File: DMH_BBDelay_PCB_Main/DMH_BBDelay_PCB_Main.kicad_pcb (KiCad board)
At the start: 2 copper layers, 99 x 175 mm, 0 parts

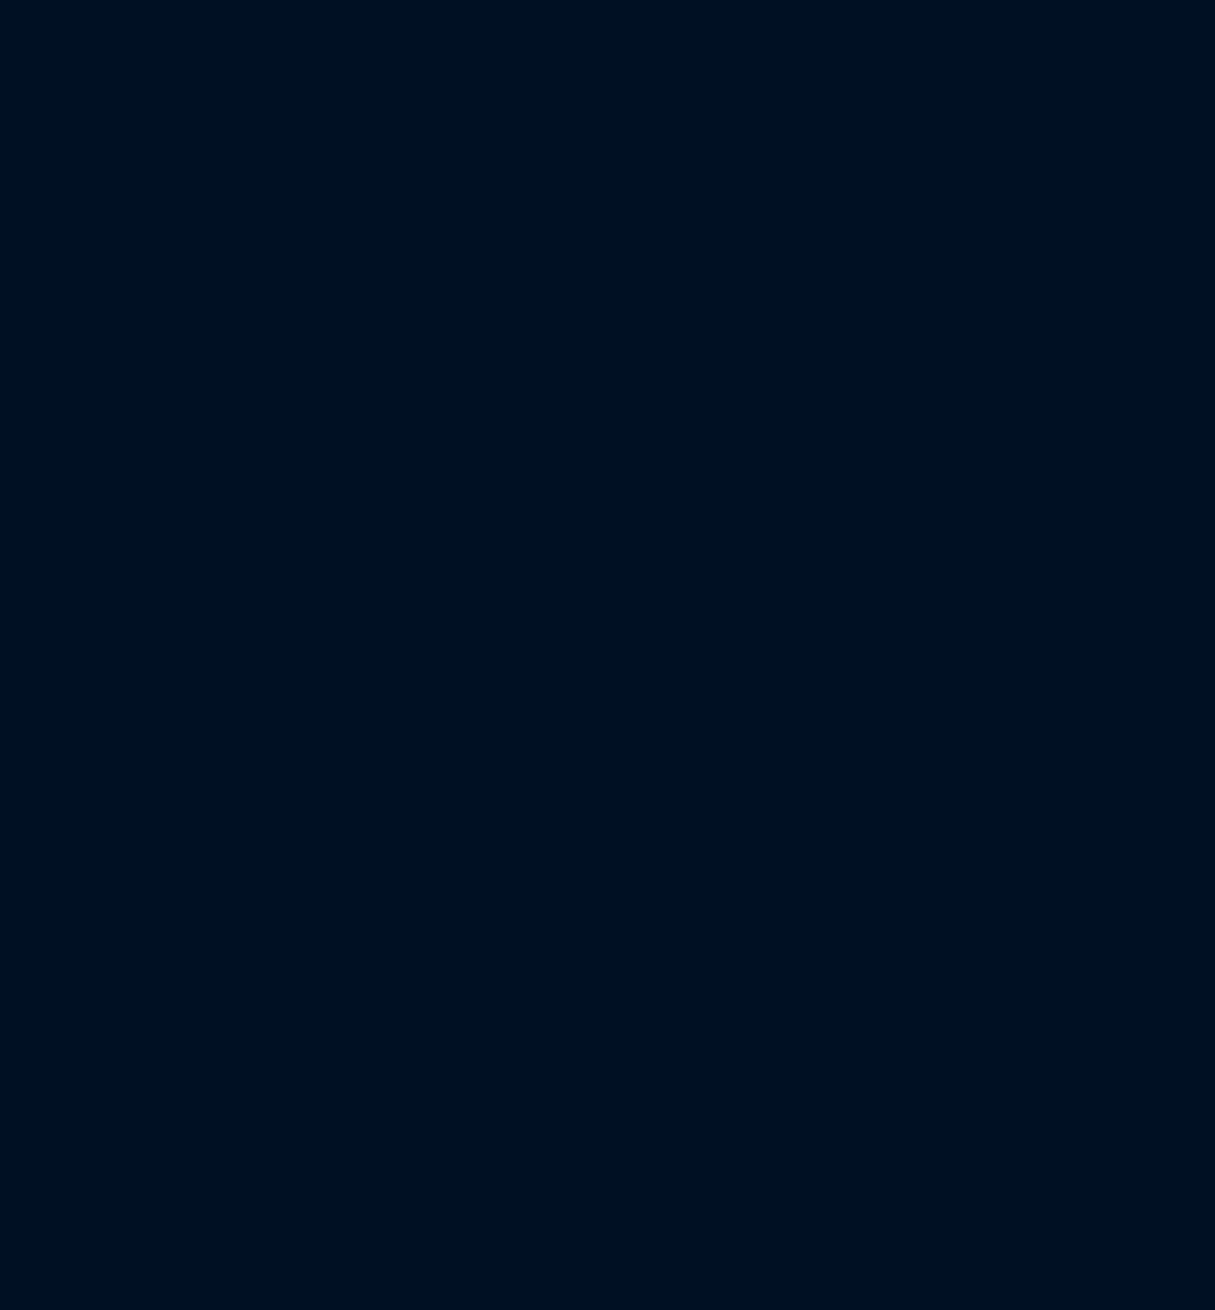
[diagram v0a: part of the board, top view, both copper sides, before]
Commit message: Added connectors for submodules
... and marked which components are not in Main PCB
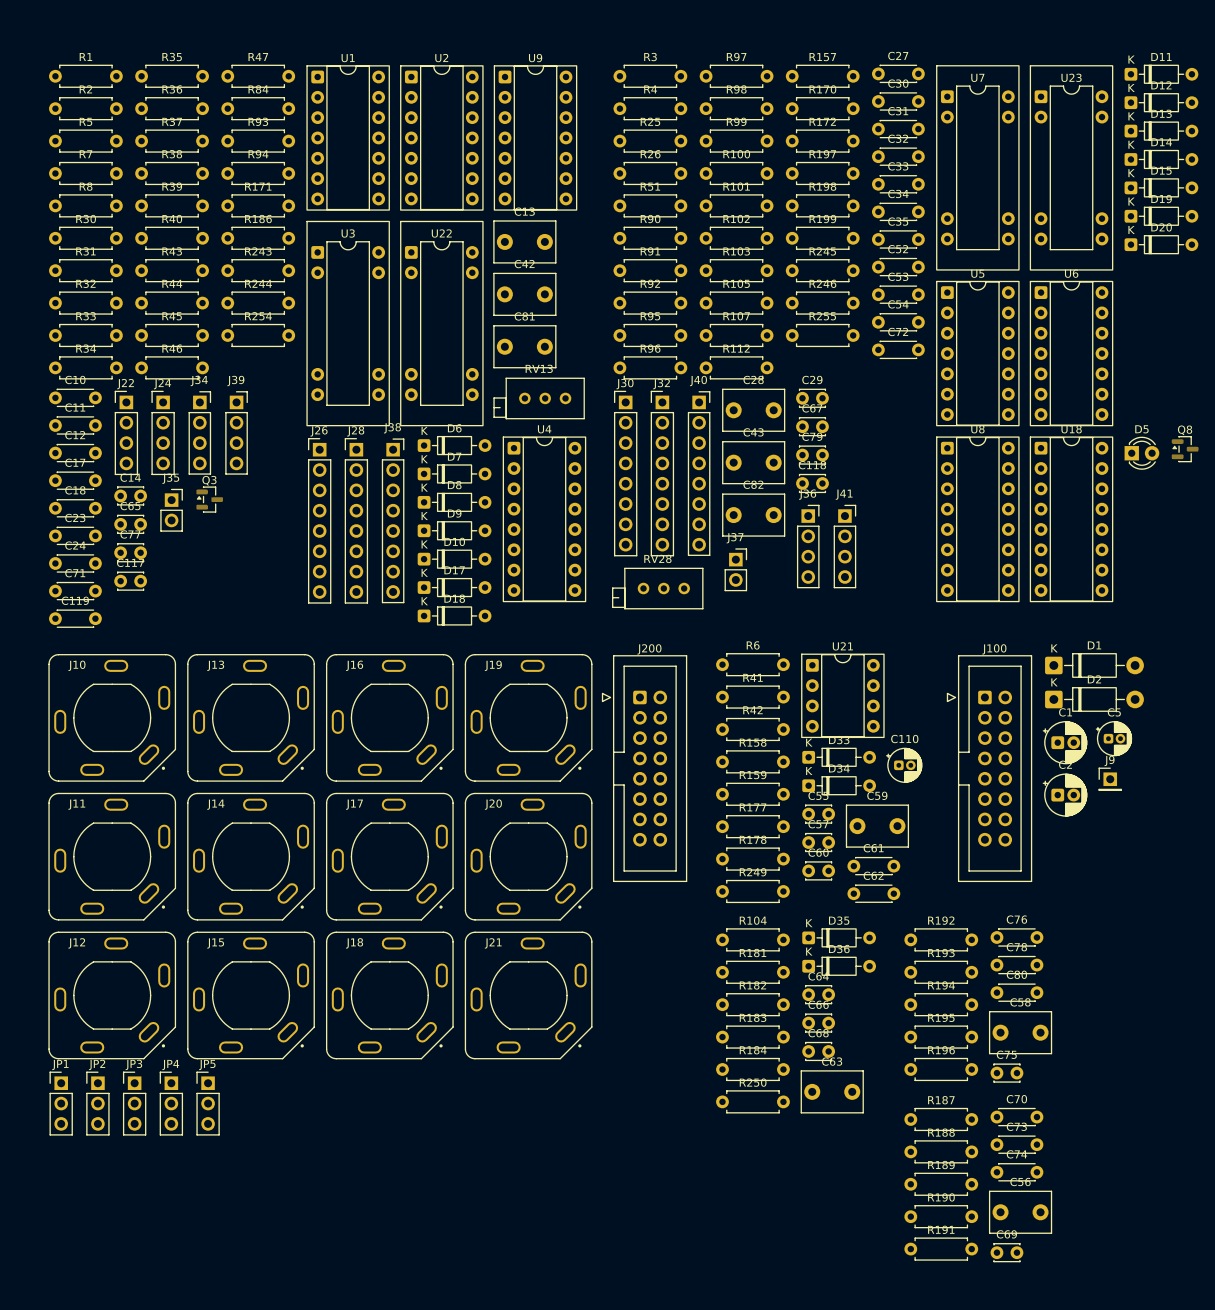
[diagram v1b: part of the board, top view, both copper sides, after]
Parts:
- added C1: 47uF, Capacitor_THT:CP_Radial_D5.0mm_P2.00mm, F.Cu at (348.9, 141.0)
- added C10: 100nF, Capacitor_THT:C_Disc_D4.3mm_W1.9mm_P5.00mm, F.Cu at (223.6, 97.9)
- added C11: 100nF, Capacitor_THT:C_Disc_D4.3mm_W1.9mm_P5.00mm, F.Cu at (223.6, 101.4)
- added C110: 4.7uF, Capacitor_THT:CP_Radial_D4.0mm_P1.50mm, F.Cu at (329.0, 143.9)
- added C117: 100pF, Capacitor_THT:C_Disc_D3.0mm_W2.0mm_P2.50mm, F.Cu at (231.7, 120.8)
- added C118: 100pF, Capacitor_THT:C_Disc_D3.0mm_W2.0mm_P2.50mm, F.Cu at (317.0, 108.6)
- added C119: 3.3uF, Capacitor_THT:C_Disc_D4.3mm_W1.9mm_P5.00mm, F.Cu at (223.6, 125.5)
- added C12: 100nF, Capacitor_THT:C_Disc_D4.3mm_W1.9mm_P5.00mm, F.Cu at (223.6, 104.8)
- added C13: 1uF Film, Capacitor_THT:C_Disc_D7.5mm_W5.0mm_P5.00mm, F.Cu at (279.8, 78.4)
- added C14: 220pF, Capacitor_THT:C_Disc_D3.0mm_W2.0mm_P2.50mm, F.Cu at (231.7, 110.2)
- added C17: 15nF, Capacitor_THT:C_Disc_D4.3mm_W1.9mm_P5.00mm, F.Cu at (223.6, 108.3)
- added C18: 100nF, Capacitor_THT:C_Disc_D4.3mm_W1.9mm_P5.00mm, F.Cu at (223.6, 111.7)
- added C2: 47uF, Capacitor_THT:CP_Radial_D5.0mm_P2.00mm, F.Cu at (348.9, 147.6)
- added C23: 100nF, Capacitor_THT:C_Disc_D4.3mm_W1.9mm_P5.00mm, F.Cu at (223.6, 115.2)
- added C24: 100nF, Capacitor_THT:C_Disc_D4.3mm_W1.9mm_P5.00mm, F.Cu at (223.6, 118.6)
- added C27: 100nF, Capacitor_THT:C_Disc_D4.3mm_W1.9mm_P5.00mm, F.Cu at (326.4, 57.4)
- added C28: 1uF Film, Capacitor_THT:C_Disc_D7.5mm_W5.0mm_P5.00mm, F.Cu at (308.4, 99.5)
- added C29: 220pF, Capacitor_THT:C_Disc_D3.0mm_W2.0mm_P2.50mm, F.Cu at (317.0, 98.0)
- added C30: 100nF, Capacitor_THT:C_Disc_D4.3mm_W1.9mm_P5.00mm, F.Cu at (326.4, 60.9)
- added C31: 100nF, Capacitor_THT:C_Disc_D4.3mm_W1.9mm_P5.00mm, F.Cu at (326.4, 64.3)
- added C32: 15nF, Capacitor_THT:C_Disc_D4.3mm_W1.9mm_P5.00mm, F.Cu at (326.4, 67.8)
- added C33: 100nF, Capacitor_THT:C_Disc_D4.3mm_W1.9mm_P5.00mm, F.Cu at (326.4, 71.2)
- added C34: 100nF, Capacitor_THT:C_Disc_D4.3mm_W1.9mm_P5.00mm, F.Cu at (326.4, 74.7)
- added C35: 100nF, Capacitor_THT:C_Disc_D4.3mm_W1.9mm_P5.00mm, F.Cu at (326.4, 78.1)
- added C42: 1uF Film, Capacitor_THT:C_Disc_D7.5mm_W5.0mm_P5.00mm, F.Cu at (279.8, 85.0)
- added C43: 1uF Film, Capacitor_THT:C_Disc_D7.5mm_W5.0mm_P5.00mm, F.Cu at (308.4, 106.0)
- added C5: 47uF, Capacitor_THT:CP_Radial_D4.0mm_P1.50mm, F.Cu at (355.2, 140.5)
- added C52: 100nF, Capacitor_THT:C_Disc_D4.3mm_W1.9mm_P5.00mm, F.Cu at (326.4, 81.6)
- added C53: 100nF, Capacitor_THT:C_Disc_D4.3mm_W1.9mm_P5.00mm, F.Cu at (326.4, 85.0)
- added C54: 100nF, Capacitor_THT:C_Disc_D4.3mm_W1.9mm_P5.00mm, F.Cu at (326.4, 88.5)
- added C55: 150p, Capacitor_THT:C_Disc_D3.0mm_W2.0mm_P2.50mm, F.Cu at (317.7, 150.0)
- added C56: 1uF Film, Capacitor_THT:C_Disc_D7.5mm_W5.0mm_P5.00mm, F.Cu at (341.7, 199.7)
- added C57: 1.5nF, Capacitor_THT:C_Disc_D3.0mm_W2.0mm_P2.50mm, F.Cu at (317.7, 153.5)
- added C58: 1uF Film, Capacitor_THT:C_Disc_D7.5mm_W5.0mm_P5.00mm, F.Cu at (341.7, 177.3)
- added C59: 1uF Film, Capacitor_THT:C_Disc_D7.5mm_W5.0mm_P5.00mm, F.Cu at (323.8, 151.5)
- added C60: 1.5nF, Capacitor_THT:C_Disc_D3.0mm_W2.0mm_P2.50mm, F.Cu at (317.7, 157.1)
- added C61: 100nF, Capacitor_THT:C_Disc_D4.3mm_W1.9mm_P5.00mm, F.Cu at (323.4, 156.5)
- added C62: 100nF, Capacitor_THT:C_Disc_D4.3mm_W1.9mm_P5.00mm, F.Cu at (323.4, 159.9)
- added C63: 1uF Film, Capacitor_THT:C_Disc_D7.5mm_W5.0mm_P5.00mm, F.Cu at (318.2, 184.7)
- added C64: 1.5nF, Capacitor_THT:C_Disc_D3.0mm_W2.0mm_P2.50mm, F.Cu at (317.7, 172.5)
- added C65: 1nF, Capacitor_THT:C_Disc_D3.0mm_W2.0mm_P2.50mm, F.Cu at (231.7, 113.7)
- added C66: 1.5nF, Capacitor_THT:C_Disc_D3.0mm_W2.0mm_P2.50mm, F.Cu at (317.7, 176.1)
- added C67: 1nF, Capacitor_THT:C_Disc_D3.0mm_W2.0mm_P2.50mm, F.Cu at (317.0, 101.5)
- added C68: 150p, Capacitor_THT:C_Disc_D3.0mm_W2.0mm_P2.50mm, F.Cu at (317.7, 179.6)
- added C69: 100p, Capacitor_THT:C_Disc_D3.0mm_W2.0mm_P2.50mm, F.Cu at (341.3, 204.8)
- added C70: 1.5nF, Capacitor_THT:C_Disc_D4.3mm_W1.9mm_P5.00mm, F.Cu at (341.3, 187.8)
- added C71: 100nF, Capacitor_THT:C_Disc_D4.3mm_W1.9mm_P5.00mm, F.Cu at (223.6, 122.1)
- added C72: 100nF, Capacitor_THT:C_Disc_D4.3mm_W1.9mm_P5.00mm, F.Cu at (326.4, 91.9)
- added C73: 1nF, Capacitor_THT:C_Disc_D4.3mm_W1.9mm_P5.00mm, F.Cu at (341.3, 191.3)
- added C74: 1nF, Capacitor_THT:C_Disc_D4.3mm_W1.9mm_P5.00mm, F.Cu at (341.3, 194.7)
- added C75: 100p, Capacitor_THT:C_Disc_D3.0mm_W2.0mm_P2.50mm, F.Cu at (341.3, 182.3)
- added C76: 1nF, Capacitor_THT:C_Disc_D4.3mm_W1.9mm_P5.00mm, F.Cu at (341.3, 165.4)
- added C77: 220pF, Capacitor_THT:C_Disc_D3.0mm_W2.0mm_P2.50mm, F.Cu at (231.7, 117.3)
- added C78: 1nF, Capacitor_THT:C_Disc_D4.3mm_W1.9mm_P5.00mm, F.Cu at (341.3, 168.8)
- added C79: 220pF, Capacitor_THT:C_Disc_D3.0mm_W2.0mm_P2.50mm, F.Cu at (317.0, 105.1)
- added C80: 1.5nF, Capacitor_THT:C_Disc_D4.3mm_W1.9mm_P5.00mm, F.Cu at (341.3, 172.3)
- added C81: 1uF Film, Capacitor_THT:C_Disc_D7.5mm_W5.0mm_P5.00mm, F.Cu at (279.8, 91.5)
- added C82: 1uF Film, Capacitor_THT:C_Disc_D7.5mm_W5.0mm_P5.00mm, F.Cu at (308.4, 112.6)
- added D1: 1N5819, Diode_THT:D_DO-41_SOD81_P10.16mm_Horizontal, F.Cu at (348.4, 131.4)
- added D10: ZPD5v1, Diode_THT:D_DO-35_SOD27_P7.62mm_Horizontal, F.Cu at (269.7, 118.1)
- added D11: BAT85, Diode_THT:D_DO-35_SOD27_P7.62mm_Horizontal, F.Cu at (358.0, 57.5)
- added D12: ZPD5v1, Diode_THT:D_DO-35_SOD27_P7.62mm_Horizontal, F.Cu at (358.0, 61.0)
- added D13: BAT85, Diode_THT:D_DO-35_SOD27_P7.62mm_Horizontal, F.Cu at (358.0, 64.6)
- added D14: ZPD5v1, Diode_THT:D_DO-35_SOD27_P7.62mm_Horizontal, F.Cu at (358.0, 68.1)
- added D15: 1N4148, Diode_THT:D_DO-35_SOD27_P7.62mm_Horizontal, F.Cu at (358.0, 71.7)
- added D17: ZPD3v0, Diode_THT:D_DO-35_SOD27_P7.62mm_Horizontal, F.Cu at (269.7, 121.6)
- added D18: ZPD3v0, Diode_THT:D_DO-35_SOD27_P7.62mm_Horizontal, F.Cu at (269.7, 125.2)
- added D19: ZPD3v0, Diode_THT:D_DO-35_SOD27_P7.62mm_Horizontal, F.Cu at (358.0, 75.2)
- added D2: 1N5819, Diode_THT:D_DO-41_SOD81_P10.16mm_Horizontal, F.Cu at (348.4, 135.6)
- added D20: ZPD3v0, Diode_THT:D_DO-35_SOD27_P7.62mm_Horizontal, F.Cu at (358.0, 78.8)
- added D33: 1N4148, Diode_THT:D_DO-35_SOD27_P7.62mm_Horizontal, F.Cu at (317.7, 142.9)
- added D34: 1N4148, Diode_THT:D_DO-35_SOD27_P7.62mm_Horizontal, F.Cu at (317.7, 146.4)
- added D35: 1N4148, Diode_THT:D_DO-35_SOD27_P7.62mm_Horizontal, F.Cu at (317.7, 165.4)
- added D36: 1N4148, Diode_THT:D_DO-35_SOD27_P7.62mm_Horizontal, F.Cu at (317.7, 169.0)
- added D5: LED_Blue, LED_THT:LED_D3.0mm, F.Cu at (358.1, 104.8)
- added D6: 1N4148, Diode_THT:D_DO-35_SOD27_P7.62mm_Horizontal, F.Cu at (269.7, 103.9)
- added D7: ZPD5v1, Diode_THT:D_DO-35_SOD27_P7.62mm_Horizontal, F.Cu at (269.7, 107.4)
- added D8: BAT85, Diode_THT:D_DO-35_SOD27_P7.62mm_Horizontal, F.Cu at (269.7, 111.0)
- added D9: BAT85, Diode_THT:D_DO-35_SOD27_P7.62mm_Horizontal, F.Cu at (269.7, 114.5)
- added J10: TRS_Jack_6.35mm_Sw, SynthStuff:CUI_SJ-63083D, F.Cu at (230.7, 137.9)
- added J100: IDC_02x08, SynthStuff:IDC-Header_2x08_P2.54mm_Vertical_Eurorack, F.Cu at (339.8, 135.4)
- added J11: TRS_Jack_6.35mm_Sw, SynthStuff:CUI_SJ-63083D, F.Cu at (230.7, 155.3)
- added J12: TRS_Jack_6.35mm_Sw, SynthStuff:CUI_SJ-63083D, F.Cu at (230.7, 172.6)
- added J13: TRS_Jack_6.35mm_Sw, SynthStuff:CUI_SJ-63083D, F.Cu at (248.0, 137.9)
- added J14: TRS_Jack_6.35mm_Sw, SynthStuff:CUI_SJ-63083D, F.Cu at (248.0, 155.3)
- added J15: TRS_Jack_6.35mm_Sw, SynthStuff:CUI_SJ-63083D, F.Cu at (248.0, 172.6)
- added J16: TRS_Jack_6.35mm_Sw, SynthStuff:CUI_SJ-63083D, F.Cu at (265.4, 137.9)
- added J17: TRS_Jack_6.35mm_Sw, SynthStuff:CUI_SJ-63083D, F.Cu at (265.4, 155.3)
- added J18: TRS_Jack_6.35mm_Sw, SynthStuff:CUI_SJ-63083D, F.Cu at (265.4, 172.6)
- added J19: TRS_Jack_6.35mm_Sw, SynthStuff:CUI_SJ-63083D, F.Cu at (282.7, 137.9)
- added J20: TRS_Jack_6.35mm_Sw, SynthStuff:CUI_SJ-63083D, F.Cu at (282.7, 155.3)
- added J200: IDC_02x08, SynthStuff:IDC-Header_2x08_P2.54mm_Vertical_BackBone, F.Cu at (296.6, 135.4)
- added J21: TRS_Jack_6.35mm_Sw, SynthStuff:CUI_SJ-63083D, F.Cu at (282.7, 172.6)
- added J22: Conn_01x04, Connector_PinHeader_2.54mm:PinHeader_1x04_P2.54mm_Vertical, F.Cu at (232.4, 98.5)
- added J24: Conn_01x04, Connector_PinHeader_2.54mm:PinHeader_1x04_P2.54mm_Vertical, F.Cu at (237.0, 98.5)
- added J26: Conn_01x08, Connector_PinHeader_2.54mm:PinHeader_1x08_P2.54mm_Vertical, F.Cu at (256.6, 104.4)
- added J28: Conn_01x08, Connector_PinHeader_2.54mm:PinHeader_1x08_P2.54mm_Vertical, F.Cu at (261.2, 104.4)
- added J30: Conn_01x08, Connector_PinHeader_2.54mm:PinHeader_1x08_P2.54mm_Vertical, F.Cu at (294.9, 98.5)
- added J32: Conn_01x08, Connector_PinHeader_2.54mm:PinHeader_1x08_P2.54mm_Vertical, F.Cu at (299.4, 98.5)
- added J34: Conn_01x04, Connector_PinSocket_2.54mm:PinSocket_1x04_P2.54mm_Vertical, F.Cu at (241.6, 98.5)
- added J35: Conn_01x02, Connector_PinSocket_2.54mm:PinSocket_1x02_P2.54mm_Vertical, F.Cu at (238.1, 110.7)
- added J36: Conn_01x04, Connector_PinSocket_2.54mm:PinSocket_1x04_P2.54mm_Vertical, F.Cu at (317.7, 112.7)
- added J37: Conn_01x02, Connector_PinSocket_2.54mm:PinSocket_1x02_P2.54mm_Vertical, F.Cu at (308.6, 118.1)
- added J38: Conn_01x08, Connector_PinSocket_2.54mm:PinSocket_1x08_P2.54mm_Vertical, F.Cu at (265.8, 104.4)
- added J39: Conn_01x04, Connector_PinSocket_2.54mm:PinSocket_1x04_P2.54mm_Vertical, F.Cu at (246.2, 98.5)
- added J40: Conn_01x08, Connector_PinSocket_2.54mm:PinSocket_1x08_P2.54mm_Vertical, F.Cu at (304.0, 98.5)
- added J41: Conn_01x04, Connector_PinSocket_2.54mm:PinSocket_1x04_P2.54mm_Vertical, F.Cu at (322.3, 112.7)
- added J9: Conn_01x01, Connector_PinHeader_2.54mm:PinHeader_1x01_P2.54mm_Vertical, F.Cu at (355.4, 145.6)
- added JP1: Jumper_3_Bridged12, Connector_PinHeader_2.54mm:PinHeader_1x03_P2.54mm_Vertical, F.Cu at (224.3, 183.6)
- added JP2: Jumper_3_Bridged12, Connector_PinHeader_2.54mm:PinHeader_1x03_P2.54mm_Vertical, F.Cu at (228.9, 183.6)
- added JP3: Jumper_3_Bridged12, Connector_PinHeader_2.54mm:PinHeader_1x03_P2.54mm_Vertical, F.Cu at (233.5, 183.6)
- added JP4: Jumper_3_Bridged12, Connector_PinHeader_2.54mm:PinHeader_1x03_P2.54mm_Vertical, F.Cu at (238.1, 183.6)
- added JP5: Jumper_3_Bridged12, Connector_PinHeader_2.54mm:PinHeader_1x03_P2.54mm_Vertical, F.Cu at (242.7, 183.6)
- added Q3: J113, Package_TO_SOT_SMD:SOT-23, F.Cu at (242.8, 110.6)
- added Q8: J113, Package_TO_SOT_SMD:SOT-23, F.Cu at (364.8, 104.3)
- added R1: 220k, Resistor_THT:R_Axial_DIN0207_L6.3mm_D2.5mm_P7.62mm_Horizontal, F.Cu at (223.6, 57.7)
- added R100: 1k, Resistor_THT:R_Axial_DIN0207_L6.3mm_D2.5mm_P7.62mm_Horizontal, F.Cu at (304.9, 69.9)
- added R101: 100k, Resistor_THT:R_Axial_DIN0207_L6.3mm_D2.5mm_P7.62mm_Horizontal, F.Cu at (304.9, 73.9)
- added R102: 10k, Resistor_THT:R_Axial_DIN0207_L6.3mm_D2.5mm_P7.62mm_Horizontal, F.Cu at (304.9, 78.0)
- added R103: 39k, Resistor_THT:R_Axial_DIN0207_L6.3mm_D2.5mm_P7.62mm_Horizontal, F.Cu at (304.9, 82.0)
- added R104: 100k, Resistor_THT:R_Axial_DIN0207_L6.3mm_D2.5mm_P7.62mm_Horizontal, F.Cu at (307.0, 165.7)
- added R105: 10k, Resistor_THT:R_Axial_DIN0207_L6.3mm_D2.5mm_P7.62mm_Horizontal, F.Cu at (304.9, 86.1)
- added R107: 39k, Resistor_THT:R_Axial_DIN0207_L6.3mm_D2.5mm_P7.62mm_Horizontal, F.Cu at (304.9, 90.1)
- added R112: 1k, Resistor_THT:R_Axial_DIN0207_L6.3mm_D2.5mm_P7.62mm_Horizontal, F.Cu at (304.9, 94.2)
- added R157: 4k7, Resistor_THT:R_Axial_DIN0207_L6.3mm_D2.5mm_P7.62mm_Horizontal, F.Cu at (315.7, 57.7)
- added R158: 47k, Resistor_THT:R_Axial_DIN0207_L6.3mm_D2.5mm_P7.62mm_Horizontal, F.Cu at (307.0, 143.4)
- added R159: 56k, Resistor_THT:R_Axial_DIN0207_L6.3mm_D2.5mm_P7.62mm_Horizontal, F.Cu at (307.0, 147.5)
- added R170: 100k, Resistor_THT:R_Axial_DIN0207_L6.3mm_D2.5mm_P7.62mm_Horizontal, F.Cu at (315.7, 61.8)
- added R171: 100k, Resistor_THT:R_Axial_DIN0207_L6.3mm_D2.5mm_P7.62mm_Horizontal, F.Cu at (245.1, 73.9)
- added R172: 100k, Resistor_THT:R_Axial_DIN0207_L6.3mm_D2.5mm_P7.62mm_Horizontal, F.Cu at (315.7, 65.8)
- added R177: 33k, Resistor_THT:R_Axial_DIN0207_L6.3mm_D2.5mm_P7.62mm_Horizontal, F.Cu at (307.0, 151.5)
- added R178: 100k, Resistor_THT:R_Axial_DIN0207_L6.3mm_D2.5mm_P7.62mm_Horizontal, F.Cu at (307.0, 155.6)
- added R181: 47k, Resistor_THT:R_Axial_DIN0207_L6.3mm_D2.5mm_P7.62mm_Horizontal, F.Cu at (307.0, 169.7)
- added R182: 56k, Resistor_THT:R_Axial_DIN0207_L6.3mm_D2.5mm_P7.62mm_Horizontal, F.Cu at (307.0, 173.8)
- added R183: 100k, Resistor_THT:R_Axial_DIN0207_L6.3mm_D2.5mm_P7.62mm_Horizontal, F.Cu at (307.0, 177.8)
- added R184: 33k, Resistor_THT:R_Axial_DIN0207_L6.3mm_D2.5mm_P7.62mm_Horizontal, F.Cu at (307.0, 181.9)
- added R186: 100R, Resistor_THT:R_Axial_DIN0207_L6.3mm_D2.5mm_P7.62mm_Horizontal, F.Cu at (245.1, 78.0)
- added R187: 120k, Resistor_THT:R_Axial_DIN0207_L6.3mm_D2.5mm_P7.62mm_Horizontal, F.Cu at (330.5, 188.1)
- added R188: 33k, Resistor_THT:R_Axial_DIN0207_L6.3mm_D2.5mm_P7.62mm_Horizontal, F.Cu at (330.5, 192.2)
- added R189: 39k, Resistor_THT:R_Axial_DIN0207_L6.3mm_D2.5mm_P7.62mm_Horizontal, F.Cu at (330.5, 196.2)
- added R190: 43k, Resistor_THT:R_Axial_DIN0207_L6.3mm_D2.5mm_P7.62mm_Horizontal, F.Cu at (330.5, 200.3)
- added R191: 43k, Resistor_THT:R_Axial_DIN0207_L6.3mm_D2.5mm_P7.62mm_Horizontal, F.Cu at (330.5, 204.3)
- added R192: 120k, Resistor_THT:R_Axial_DIN0207_L6.3mm_D2.5mm_P7.62mm_Horizontal, F.Cu at (330.5, 165.7)
- added R193: 43k, Resistor_THT:R_Axial_DIN0207_L6.3mm_D2.5mm_P7.62mm_Horizontal, F.Cu at (330.5, 169.7)
- added R194: 43k, Resistor_THT:R_Axial_DIN0207_L6.3mm_D2.5mm_P7.62mm_Horizontal, F.Cu at (330.5, 173.8)
- added R195: 39k, Resistor_THT:R_Axial_DIN0207_L6.3mm_D2.5mm_P7.62mm_Horizontal, F.Cu at (330.5, 177.8)
- added R196: 33k, Resistor_THT:R_Axial_DIN0207_L6.3mm_D2.5mm_P7.62mm_Horizontal, F.Cu at (330.5, 181.9)
- added R197: 100R, Resistor_THT:R_Axial_DIN0207_L6.3mm_D2.5mm_P7.62mm_Horizontal, F.Cu at (315.7, 69.9)
- added R198: 47k, Resistor_THT:R_Axial_DIN0207_L6.3mm_D2.5mm_P7.62mm_Horizontal, F.Cu at (315.7, 73.9)
- added R199: 47k, Resistor_THT:R_Axial_DIN0207_L6.3mm_D2.5mm_P7.62mm_Horizontal, F.Cu at (315.7, 78.0)
- added R2: 100k, Resistor_THT:R_Axial_DIN0207_L6.3mm_D2.5mm_P7.62mm_Horizontal, F.Cu at (223.6, 61.8)
- added R243: 100k, Resistor_THT:R_Axial_DIN0207_L6.3mm_D2.5mm_P7.62mm_Horizontal, F.Cu at (245.1, 82.0)
- added R244: 20k, Resistor_THT:R_Axial_DIN0207_L6.3mm_D2.5mm_P7.62mm_Horizontal, F.Cu at (245.1, 86.1)
- added R245: 20k, Resistor_THT:R_Axial_DIN0207_L6.3mm_D2.5mm_P7.62mm_Horizontal, F.Cu at (315.7, 82.0)
- added R246: 100k, Resistor_THT:R_Axial_DIN0207_L6.3mm_D2.5mm_P7.62mm_Horizontal, F.Cu at (315.7, 86.1)
- added R249: 1k, Resistor_THT:R_Axial_DIN0207_L6.3mm_D2.5mm_P7.62mm_Horizontal, F.Cu at (307.0, 159.6)
- added R25: 100k, Resistor_THT:R_Axial_DIN0207_L6.3mm_D2.5mm_P7.62mm_Horizontal, F.Cu at (294.1, 65.8)
- added R250: 1k, Resistor_THT:R_Axial_DIN0207_L6.3mm_D2.5mm_P7.62mm_Horizontal, F.Cu at (307.0, 185.9)
- added R254: 1k, Resistor_THT:R_Axial_DIN0207_L6.3mm_D2.5mm_P7.62mm_Horizontal, F.Cu at (245.1, 90.1)
- added R255: 1k, Resistor_THT:R_Axial_DIN0207_L6.3mm_D2.5mm_P7.62mm_Horizontal, F.Cu at (315.7, 90.1)
- added R26: 2k, Resistor_THT:R_Axial_DIN0207_L6.3mm_D2.5mm_P7.62mm_Horizontal, F.Cu at (294.1, 69.9)
- added R3: 220k, Resistor_THT:R_Axial_DIN0207_L6.3mm_D2.5mm_P7.62mm_Horizontal, F.Cu at (294.1, 57.7)
- added R30: 4k7, Resistor_THT:R_Axial_DIN0207_L6.3mm_D2.5mm_P7.62mm_Horizontal, F.Cu at (223.6, 78.0)
- added R31: 56k, Resistor_THT:R_Axial_DIN0207_L6.3mm_D2.5mm_P7.62mm_Horizontal, F.Cu at (223.6, 82.0)
- added R32: 100k, Resistor_THT:R_Axial_DIN0207_L6.3mm_D2.5mm_P7.62mm_Horizontal, F.Cu at (223.6, 86.1)
- added R33: 100k, Resistor_THT:R_Axial_DIN0207_L6.3mm_D2.5mm_P7.62mm_Horizontal, F.Cu at (223.6, 90.1)
- added R34: 100k, Resistor_THT:R_Axial_DIN0207_L6.3mm_D2.5mm_P7.62mm_Horizontal, F.Cu at (223.6, 94.2)
- added R35: 6k2, Resistor_THT:R_Axial_DIN0207_L6.3mm_D2.5mm_P7.62mm_Horizontal, F.Cu at (234.3, 57.7)
- added R36: 10k, Resistor_THT:R_Axial_DIN0207_L6.3mm_D2.5mm_P7.62mm_Horizontal, F.Cu at (234.3, 61.8)
- added R37: 100k, Resistor_THT:R_Axial_DIN0207_L6.3mm_D2.5mm_P7.62mm_Horizontal, F.Cu at (234.3, 65.8)
- added R38: 39k, Resistor_THT:R_Axial_DIN0207_L6.3mm_D2.5mm_P7.62mm_Horizontal, F.Cu at (234.3, 69.9)
- added R39: 2M2, Resistor_THT:R_Axial_DIN0207_L6.3mm_D2.5mm_P7.62mm_Horizontal, F.Cu at (234.3, 73.9)
- added R4: 100k, Resistor_THT:R_Axial_DIN0207_L6.3mm_D2.5mm_P7.62mm_Horizontal, F.Cu at (294.1, 61.8)
- added R40: 10k, Resistor_THT:R_Axial_DIN0207_L6.3mm_D2.5mm_P7.62mm_Horizontal, F.Cu at (234.3, 78.0)
- added R41: 20k, Resistor_THT:R_Axial_DIN0207_L6.3mm_D2.5mm_P7.62mm_Horizontal, F.Cu at (307.0, 135.3)
- added R42: 22k, Resistor_THT:R_Axial_DIN0207_L6.3mm_D2.5mm_P7.62mm_Horizontal, F.Cu at (307.0, 139.4)
- added R43: 1k, Resistor_THT:R_Axial_DIN0207_L6.3mm_D2.5mm_P7.62mm_Horizontal, F.Cu at (234.3, 82.0)
- added R44: 10k, Resistor_THT:R_Axial_DIN0207_L6.3mm_D2.5mm_P7.62mm_Horizontal, F.Cu at (234.3, 86.1)
- added R45: 10k, Resistor_THT:R_Axial_DIN0207_L6.3mm_D2.5mm_P7.62mm_Horizontal, F.Cu at (234.3, 90.1)
- added R46: 39k, Resistor_THT:R_Axial_DIN0207_L6.3mm_D2.5mm_P7.62mm_Horizontal, F.Cu at (234.3, 94.2)
- added R47: 39k, Resistor_THT:R_Axial_DIN0207_L6.3mm_D2.5mm_P7.62mm_Horizontal, F.Cu at (245.1, 57.7)
- added R5: 100k, Resistor_THT:R_Axial_DIN0207_L6.3mm_D2.5mm_P7.62mm_Horizontal, F.Cu at (223.6, 65.8)
- added R51: 10k, Resistor_THT:R_Axial_DIN0207_L6.3mm_D2.5mm_P7.62mm_Horizontal, F.Cu at (294.1, 73.9)
- added R6: 100k, Resistor_THT:R_Axial_DIN0207_L6.3mm_D2.5mm_P7.62mm_Horizontal, F.Cu at (307.0, 131.3)
- added R7: 3k3, Resistor_THT:R_Axial_DIN0207_L6.3mm_D2.5mm_P7.62mm_Horizontal, F.Cu at (223.6, 69.9)
- added R8: 2k, Resistor_THT:R_Axial_DIN0207_L6.3mm_D2.5mm_P7.62mm_Horizontal, F.Cu at (223.6, 73.9)
- added R84: 1k, Resistor_THT:R_Axial_DIN0207_L6.3mm_D2.5mm_P7.62mm_Horizontal, F.Cu at (245.1, 61.8)
- added R90: 3k3, Resistor_THT:R_Axial_DIN0207_L6.3mm_D2.5mm_P7.62mm_Horizontal, F.Cu at (294.1, 78.0)
- added R91: 39k, Resistor_THT:R_Axial_DIN0207_L6.3mm_D2.5mm_P7.62mm_Horizontal, F.Cu at (294.1, 82.0)
- added R92: 2M2, Resistor_THT:R_Axial_DIN0207_L6.3mm_D2.5mm_P7.62mm_Horizontal, F.Cu at (294.1, 86.1)
- added R93: 47k, Resistor_THT:R_Axial_DIN0207_L6.3mm_D2.5mm_P7.62mm_Horizontal, F.Cu at (245.1, 65.8)
- added R94: 47k, Resistor_THT:R_Axial_DIN0207_L6.3mm_D2.5mm_P7.62mm_Horizontal, F.Cu at (245.1, 69.9)
- added R95: 100k, Resistor_THT:R_Axial_DIN0207_L6.3mm_D2.5mm_P7.62mm_Horizontal, F.Cu at (294.1, 90.1)
- added R96: 100k, Resistor_THT:R_Axial_DIN0207_L6.3mm_D2.5mm_P7.62mm_Horizontal, F.Cu at (294.1, 94.2)
- added R97: 100k, Resistor_THT:R_Axial_DIN0207_L6.3mm_D2.5mm_P7.62mm_Horizontal, F.Cu at (304.9, 57.7)
- added R98: 10k, Resistor_THT:R_Axial_DIN0207_L6.3mm_D2.5mm_P7.62mm_Horizontal, F.Cu at (304.9, 61.8)
- added R99: 6k2, Resistor_THT:R_Axial_DIN0207_L6.3mm_D2.5mm_P7.62mm_Horizontal, F.Cu at (304.9, 65.8)
- added RV13: 2k, Potentiometer_THT:Potentiometer_Bourns_3296X_Horizontal, F.Cu at (287.3, 98.0)
- added RV28: 2k, Potentiometer_THT:Potentiometer_Bourns_3296X_Horizontal, F.Cu at (302.2, 121.8)
- added U1: TL074, Package_DIP:DIP-14_W7.62mm_Socket, F.Cu at (256.4, 57.8)
- added U18: CD4053B, Package_DIP:DIP-16_W7.62mm_Socket, F.Cu at (346.8, 104.2)
- added U2: TL074, Package_DIP:DIP-14_W7.62mm_Socket, F.Cu at (268.1, 57.8)
- added U21: TL072, Package_DIP:DIP-8_W7.62mm_Socket, F.Cu at (318.2, 131.4)
- added U22: V3205, Package_DIP:DIP-8-16_W7.62mm_Socket, F.Cu at (268.1, 79.7)
- added U23: V3205, Package_DIP:DIP-8-16_W7.62mm_Socket, F.Cu at (346.8, 60.3)
- added U3: V3205, Package_DIP:DIP-8-16_W7.62mm_Socket, F.Cu at (256.4, 79.7)
- added U4: CD4046, Package_DIP:DIP-16_W7.62mm_Socket, F.Cu at (280.9, 104.2)
- added U5: TL074, Package_DIP:DIP-14_W7.62mm_Socket, F.Cu at (335.1, 84.8)
- added U6: TL074, Package_DIP:DIP-14_W7.62mm_Socket, F.Cu at (346.8, 84.8)
- added U7: V3205, Package_DIP:DIP-8-16_W7.62mm_Socket, F.Cu at (335.1, 60.3)
- added U8: CD4046, Package_DIP:DIP-16_W7.62mm_Socket, F.Cu at (335.1, 104.2)
- added U9: 40106, Package_DIP:DIP-14_W7.62mm_Socket, F.Cu at (279.8, 57.8)

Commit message: Sent footprints to PCB editor
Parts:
- added Q19: BC548, Package_TO_SOT_THT:TO-92L_Inline_Wide, F.Cu at (283.6, 222.5)
- added Q20: BC548, Package_TO_SOT_THT:TO-92L_Inline_Wide, F.Cu at (283.6, 210.8)
- added R200: 100k, Resistor_THT:R_Axial_DIN0207_L6.3mm_D2.5mm_P7.62mm_Horizontal, F.Cu at (283.7, 217.2)
- added R201: 100k, Resistor_THT:R_Axial_DIN0207_L6.3mm_D2.5mm_P7.62mm_Horizontal, F.Cu at (283.7, 205.5)
- R198, R199, R93, R94: value 47k -> 100k
- R244, R245: value 20k -> 27k
- R35, R99: value 6k2 -> 10k
- R42: value 22k -> 20k
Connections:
- C14 pad 1: Clock_A_m -> Clock_A_Inv_m
- C29 pad 1: Net-(U23-CP1) -> Clock_B_Inv_m
- R198 pad 1: Net-(U7-Out2) -> Net-(R198-Pad1)
- R198 pad 2: Net-(U23-In) -> Net-(Q19-B)
- R199 pad 1: Net-(U23-In) -> Net-(R199-Pad1)
- R199 pad 2: GND -> Net-(Q20-B)
- R93 pad 1: Net-(U3-Out2) -> Net-(Q19-C)
- R93 pad 2: Net-(U22-In) -> +5V
- R94 pad 1: Net-(U22-In) -> Net-(Q20-C)
- R94 pad 2: GND -> +5V
- U22 pad 2: Clock_A_Inv_m -> Net-(U22-CP2)
- U22 pad 6: Clock_A_m -> Clock_A_Inv_m
- U23 pad 2: Clock_B_Inv_m -> Net-(U23-CP2)
- U23 pad 6: Net-(U23-CP1) -> Clock_B_Inv_m
- U3 pad 4: Net-(U3-Out2) -> Net-(U22-In)
- U3 pad 6: Clock_A_m -> Net-(U22-CP2)
- U4 pad 14: +5V -> unconnected-(U4-SigIn-Pad14)
- U4 pad 2: Clock_A_Inv_m -> unconnected-(U4-PC1-Pad2)
- U4 pad 3: Clock_A_m -> unconnected-(U4-RefIn-Pad3)
- U4 pad 5: Net-(U4-Inh) -> Net-(Q19-C)
- U7 pad 4: Net-(U7-Out2) -> Net-(U23-In)
- U7 pad 6: Net-(U23-CP1) -> Net-(U23-CP2)
- U8 pad 5: Net-(U8-Inh) -> Net-(Q20-C)
- U9 pad 10: Net-(U4-Inh) -> Net-(U22-CP2)
- U9 pad 11: Net-(U9-Pad11) -> Clock_A_Inv_m
- U9 pad 12: Net-(U23-CP1) -> Net-(U23-CP2)
- U9 pad 3: Net-(U9-Pad3) -> Clock_A_m
- U9 pad 4: Net-(U8-Inh) -> Clock_A_Inv_m
- U9 pad 6: Net-(U9-Pad3) -> Net-(R199-Pad1)
- U9 pad 8: Net-(U9-Pad11) -> Net-(R198-Pad1)

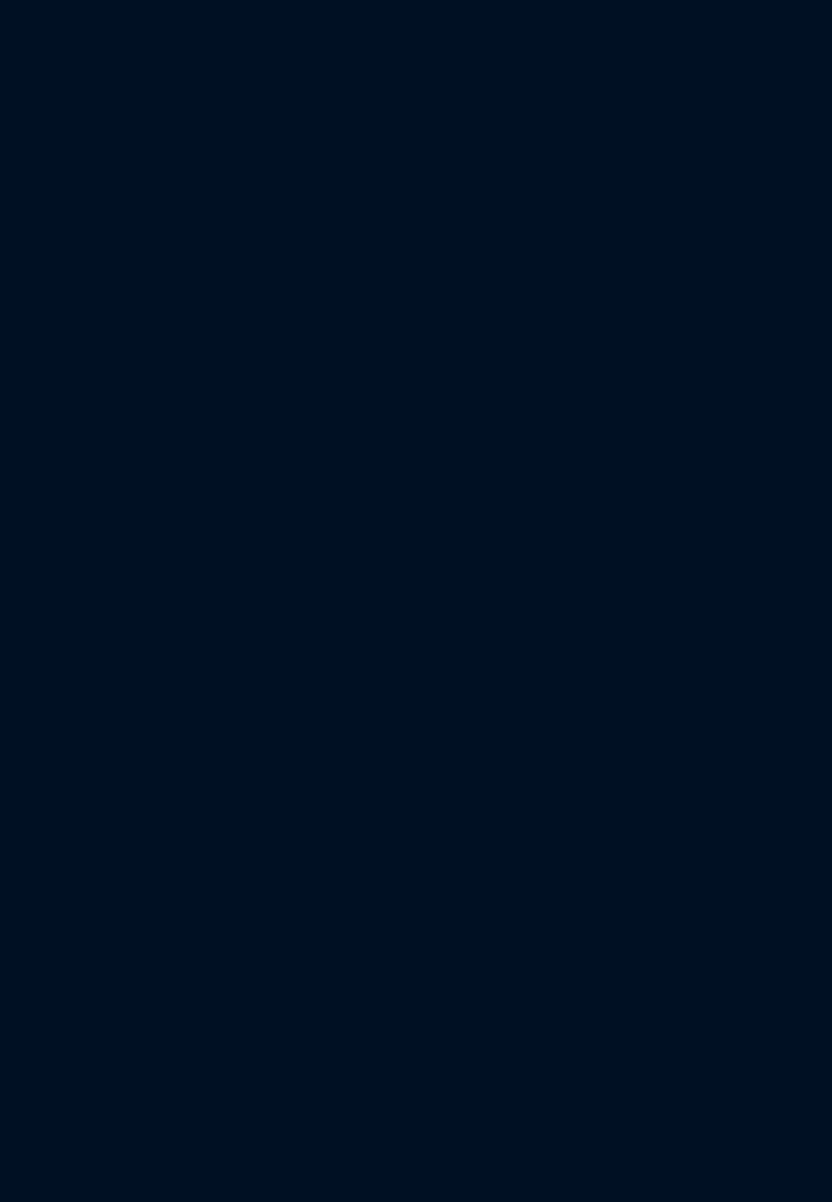
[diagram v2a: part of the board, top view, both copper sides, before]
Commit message: Added extra V3205 to channel B
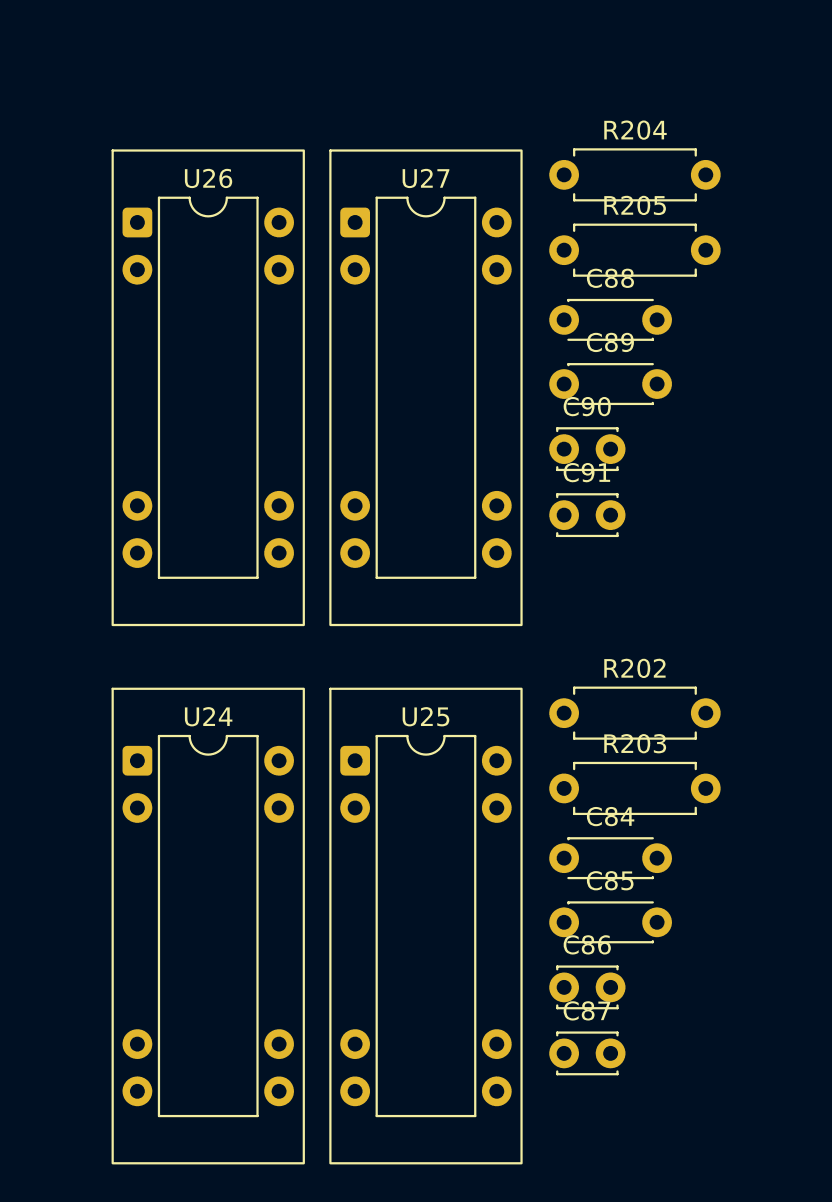
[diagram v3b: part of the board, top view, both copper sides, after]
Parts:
- added C84: 100nF, Capacitor_THT:C_Disc_D4.3mm_W1.9mm_P5.00mm, F.Cu at (256.9, 248.0)
- added C85: 100nF, Capacitor_THT:C_Disc_D4.3mm_W1.9mm_P5.00mm, F.Cu at (256.9, 251.4)
- added C86: 220pF, Capacitor_THT:C_Disc_D3.0mm_W2.0mm_P2.50mm, F.Cu at (256.9, 254.9)
- added C87: 220pF, Capacitor_THT:C_Disc_D3.0mm_W2.0mm_P2.50mm, F.Cu at (256.9, 258.5)
- added C88: 100nF, Capacitor_THT:C_Disc_D4.3mm_W1.9mm_P5.00mm, F.Cu at (256.9, 219.0)
- added C89: 100nF, Capacitor_THT:C_Disc_D4.3mm_W1.9mm_P5.00mm, F.Cu at (256.9, 222.5)
- added C90: 220pF, Capacitor_THT:C_Disc_D3.0mm_W2.0mm_P2.50mm, F.Cu at (256.9, 226.0)
- added C91: 220pF, Capacitor_THT:C_Disc_D3.0mm_W2.0mm_P2.50mm, F.Cu at (256.9, 229.5)
- added R202: 100k, Resistor_THT:R_Axial_DIN0207_L6.3mm_D2.5mm_P7.62mm_Horizontal, F.Cu at (256.9, 240.2)
- added R203: 100k, Resistor_THT:R_Axial_DIN0207_L6.3mm_D2.5mm_P7.62mm_Horizontal, F.Cu at (256.9, 244.2)
- added R204: 100k, Resistor_THT:R_Axial_DIN0207_L6.3mm_D2.5mm_P7.62mm_Horizontal, F.Cu at (256.9, 211.2)
- added R205: 100k, Resistor_THT:R_Axial_DIN0207_L6.3mm_D2.5mm_P7.62mm_Horizontal, F.Cu at (256.9, 215.3)
- added U24: V3205, Package_DIP:DIP-8-16_W7.62mm_Socket, F.Cu at (233.9, 242.7)
- added U25: V3205, Package_DIP:DIP-8-16_W7.62mm_Socket, F.Cu at (245.7, 242.7)
- added U26: V3205, Package_DIP:DIP-8-16_W7.62mm_Socket, F.Cu at (233.9, 213.8)
- added U27: V3205, Package_DIP:DIP-8-16_W7.62mm_Socket, F.Cu at (245.7, 213.8)
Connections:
- C13 pad 1: Net-(U22-Out2) -> Net-(U25-Out2)
- C28 pad 1: Net-(U23-Out2) -> Net-(U27-Out2)
- C35 pad 1: +5V -> GND
- C35 pad 2: GND -> +5V
- C72 pad 1: +5V -> GND
- C72 pad 2: GND -> +5V
- R32 pad 2: Net-(U22-Out2) -> Net-(U25-Out2)
- R95 pad 2: Net-(U23-Out2) -> Net-(U27-Out2)
